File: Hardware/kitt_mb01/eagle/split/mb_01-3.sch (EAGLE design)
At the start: 14 parts, among them IC3.01 LSM9DS1

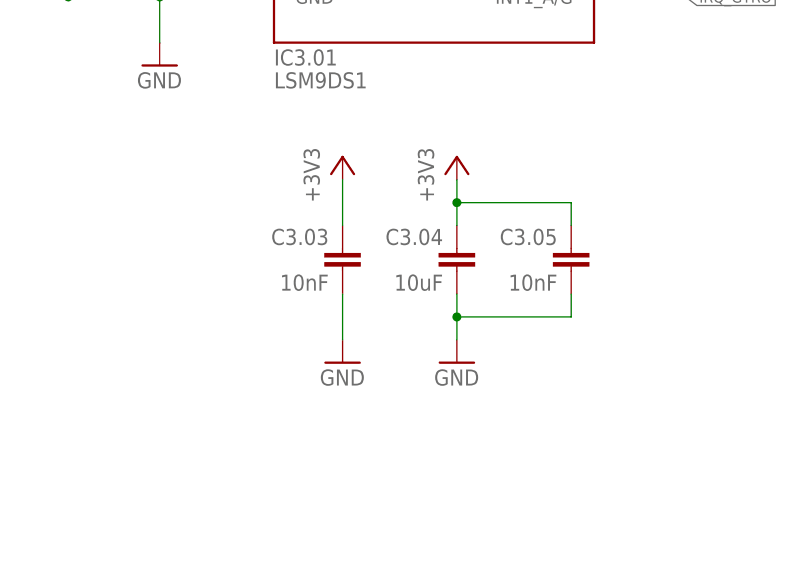
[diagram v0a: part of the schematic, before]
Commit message: did route+place for subsection 1 and 3
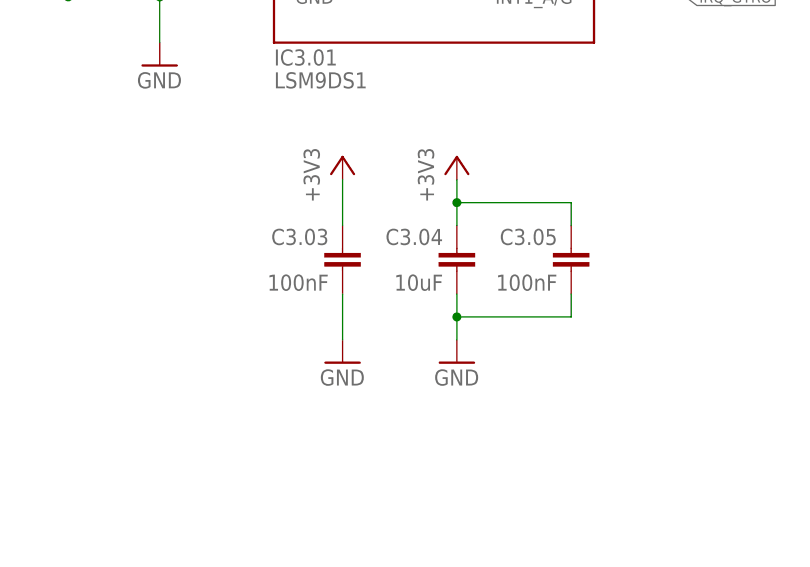
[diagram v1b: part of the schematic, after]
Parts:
- C3.03, C3.05: value 10nF -> 100nF
- C3.04: device rcl:C-EUC0603K -> resistor:C-EUC0603K
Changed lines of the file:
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@@
 <part name="C3.01" library="rcl" deviceset="C-EU" device="C0402" value="10nF"/>
 <part name="C3.02" library="rcl" deviceset="C-EU" device="C0402" value="100nF"/>
-<part name="C3.03" library="rcl" deviceset="C-EU" device="C0402" value="10nF"/>
+<part name="C3.03" library="rcl" deviceset="C-EU" device="C0402" value="100nF"/>
 <part name="GND19" library="supply1" deviceset="GND" device=""/>
 <part name="+3V2" library="supply1" deviceset="+3V3" device=""/>
-<part name="C3.04" library="rcl" deviceset="C-EU" device="C0603K" value="10uF"/>
-<part name="C3.05" library="rcl" deviceset="C-EU" device="C0402" value="10nF"/>
+<part name="C3.04" library="resistor" deviceset="C-EU" device="C0603K" value="10uF"/>
+<part name="C3.05" library="rcl" deviceset="C-EU" device="C0402" value="100nF"/>
 <part name="+3V4" library="supply1" deviceset="+3V3" device=""/>
 <part name="GND20" library="supply1" deviceset="GND" device=""/>
